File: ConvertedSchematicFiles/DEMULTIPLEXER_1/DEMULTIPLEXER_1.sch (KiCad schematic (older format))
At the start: 16 parts, among them U1 74393, U2 74151A

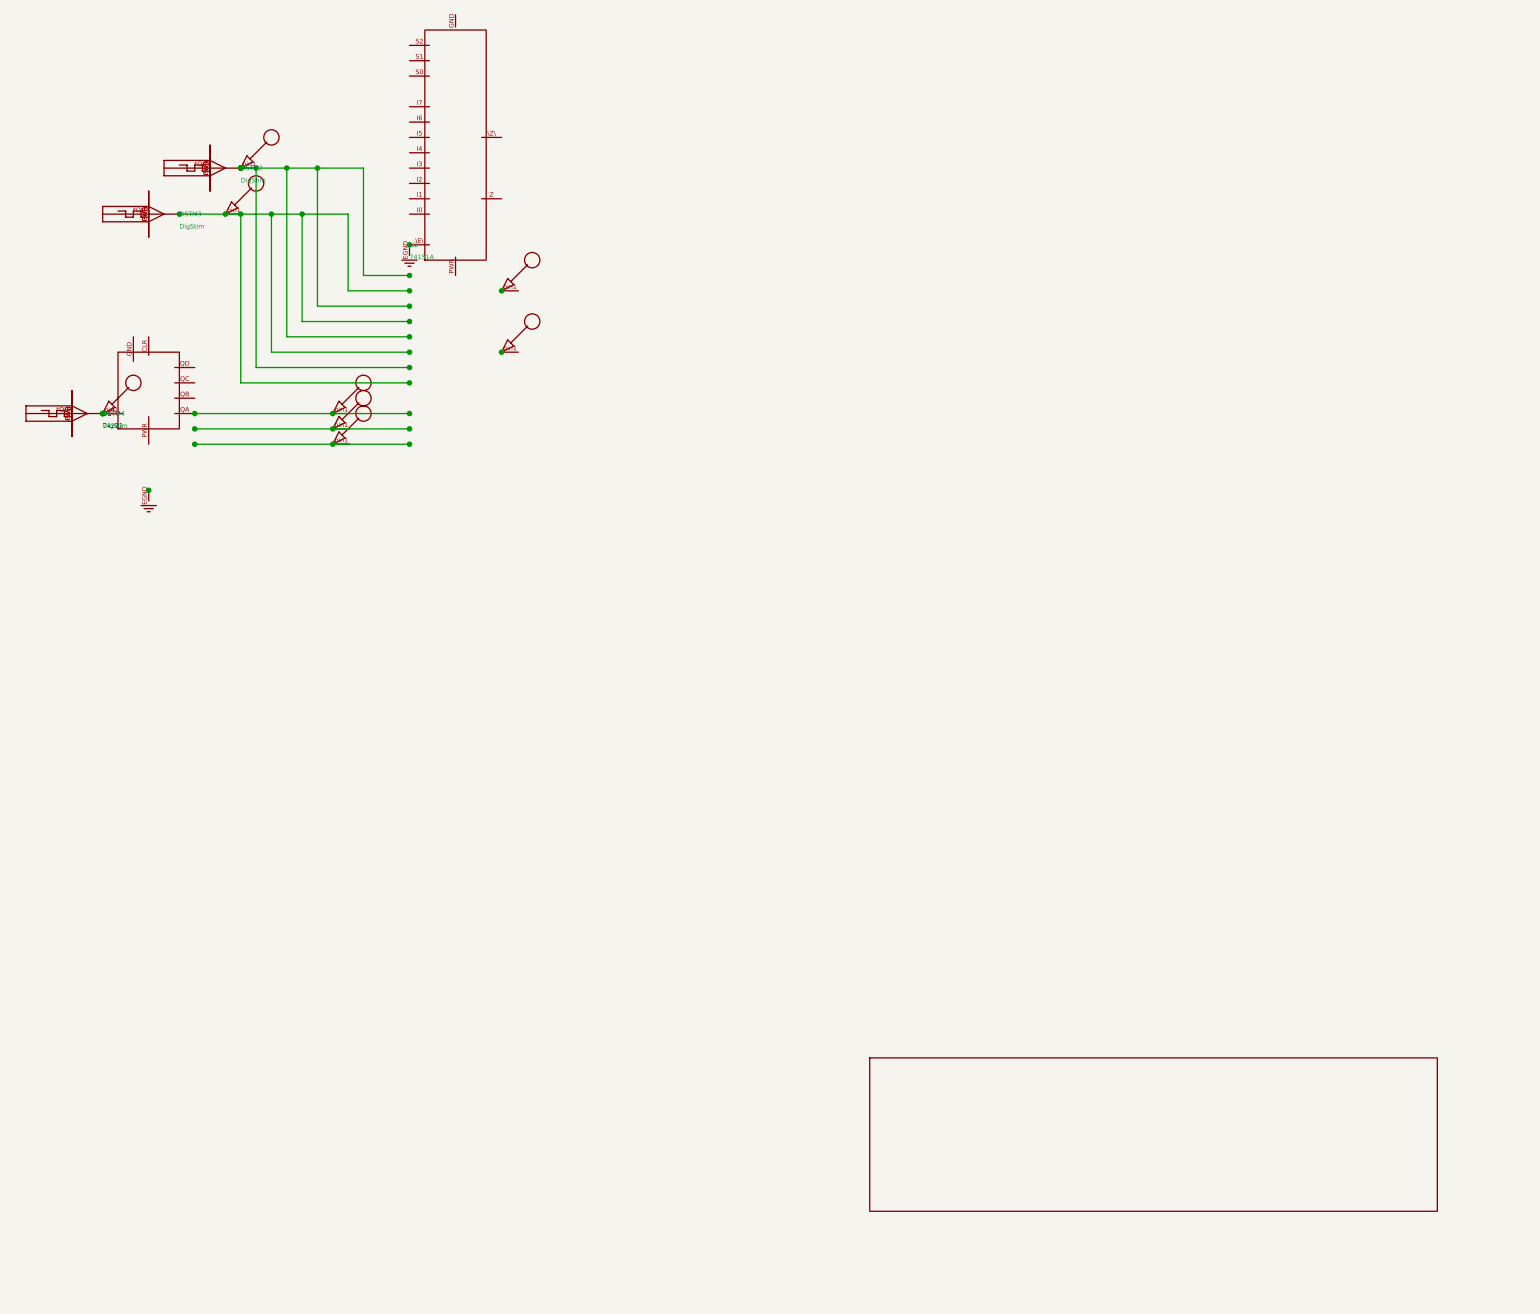
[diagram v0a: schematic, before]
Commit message: Excluded some components. These no longer appear after conversion. When calling shell commands, filenames are in "quotes"
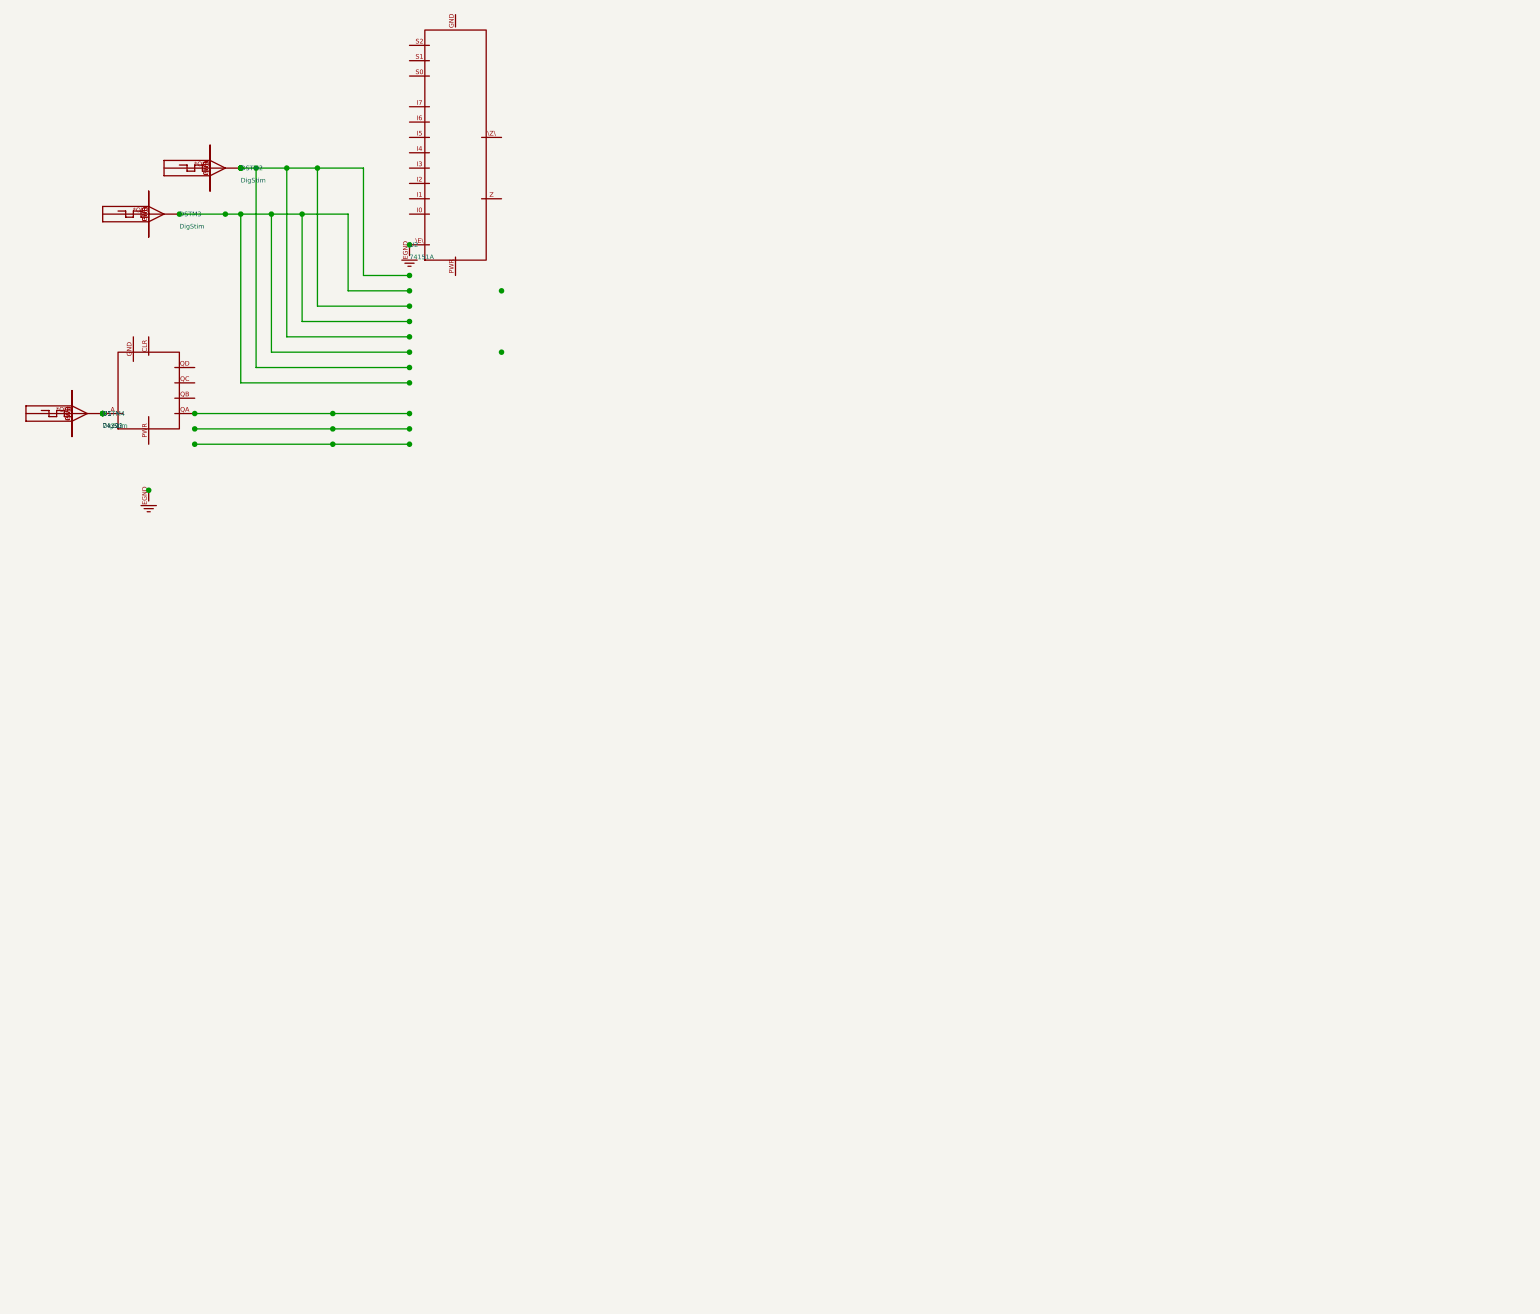
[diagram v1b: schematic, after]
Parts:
- removed nodeMarker (x8): nodeMarker, symbol NODEMARKER_PSPICE
- removed titleblk: titleblk, symbol TITLEBLK_PSPICE
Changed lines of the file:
@@
-	1    0    0    1
-$EndComp
-$Comp
-L TITLEBLK_PSPICE titleblk
-U 1 1 39760492
-P 9700 7200
-F 0 "titleblk" H 19400 14400 30  0001 L CNN
-F 1 "titleblk" H 19400 14480 30  0001 L CNN
-	1    9700 7200
-	1    0    0    1
-$EndComp
-$Comp
-L NODEMARKER_PSPICE nodeMarker
-U 1 1 66516649
-P 2500 2200
-F 0 "nodeMarker" H 5000 4400 30  0001 L CNN
-F 1 "nodeMarker" H 5000 4480 30  0001 L CNN
-	1    2500 2200
-	1    0    0    1
-$EndComp
-$Comp
-L NODEMARKER_PSPICE nodeMarker
-U 1 1 29641421
-P 2500 2100
-F 0 "nodeMarker" H 5000 4200 30  0001 L CNN
-F 1 "nodeMarker" H 5000 4280 30  0001 L CNN
-	1    2500 2100
-	1    0    0    1
-$EndComp
-$Comp
-L NODEMARKER_PSPICE nodeMarker
-U 1 1 45202362
-P 2500 2000
-F 0 "nodeMarker" H 5000 4000 30  0001 L CNN
-F 1 "nodeMarker" H 5000 4080 30  0001 L CNN
-	1    2500 2000
-	1    0    0    1
-$EndComp
-$Comp
-L NODEMARKER_PSPICE nodeMarker
-U 1 1 10490027
-P 1800 700
-F 0 "nodeMarker" H 3600 1400 30  0001 L CNN
-F 1 "nodeMarker" H 3600 1480 30  0001 L CNN
-	1    1800 700
-	1    0    0    1
-$EndComp
-$Comp
-L NODEMARKER_PSPICE nodeMarker
-U 1 1 73368690
-P 1900 400
-F 0 "nodeMarker" H 3800 800 30  0001 L CNN
-F 1 "nodeMarker" H 3800 880 30  0001 L CNN
-	1    1900 400
-	1    0    0    1
-$EndComp
-$Comp
-L NODEMARKER_PSPICE nodeMarker
-U 1 1 32520059
-P 3600 1600
-F 0 "nodeMarker" H 7200 3200 30  0001 L CNN
-F 1 "nodeMarker" H 7200 3280 30  0001 L CNN
-	1    3600 1600
-	1    0    0    1
-$EndComp
-$Comp
-L NODEMARKER_PSPICE nodeMarker
-U 1 1 74897763
-P 3600 1200
-F 0 "nodeMarker" H 7200 2400 30  0001 L CNN
-F 1 "nodeMarker" H 7200 2480 30  0001 L CNN
-	1    3600 1200
-	1    0    0    1
-$EndComp
-$Comp
-L NODEMARKER_PSPICE nodeMarker
-U 1 1 87513926
-P 1000 2000
-F 0 "nodeMarker" H 2000 4000 30  0001 L CNN
-F 1 "nodeMarker" H 2000 4080 30  0001 L CNN
-	1    1000 2000
 	1    0    0    1
 $EndComp

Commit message: Ports issue fixed. Now annotation for ports is #PWR? function added "itos"
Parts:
- removed EGND (x2): EGND, symbol EGND_PSPICE
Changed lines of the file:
@@
 $EndDescr
 $Comp
-L EGND_PSPICE EGND
+L EGND_PSPICE #PWR1
 U 1 1 14289383
 P 1300 2500
-F 0 "EGND" H 2600 5000 30  0001 L CNN
+F 0 "#PWR1" H 2600 5000 30  0001 L CNN
 F 1 "EGND" H 2600 5080 30  0001 L CNN
 	1    1300 2500
@@
 $EndComp
 $Comp
-L EGND_PSPICE EGND
+L EGND_PSPICE #PWR2
 U 1 1 46930886
 P 3000 900
-F 0 "EGND" H 6000 1800 30  0001 L CNN
+F 0 "#PWR2" H 6000 1800 30  0001 L CNN
 F 1 "EGND" H 6000 1880 30  0001 L CNN
 	1    3000 900

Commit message: Added LICENSE.txt
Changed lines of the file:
@@
 $EndDescr
 $Comp
-L EGND_PSPICE #PWR1
+L GND #PWR1
 U 1 1 14289383
 P 1300 2500
@@
 $EndComp
 $Comp
-L EGND_PSPICE #PWR2
+L GND #PWR2
 U 1 1 46930886
 P 3000 900

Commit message: Orientation fix. Library components are now inverted, with +ve y axis going up. In Schematic files, +ve y axis is downwards. This is how the KiCad libraries are. As a result of the above fixed, the converted GND is now oriented correctly.
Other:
- moved on the sheet: U1, U2
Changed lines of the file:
@@
 F 1 "EGND" H 2600 5080 30  0001 L CNN
 	1    1300 2500
-	1    0    0    1
+	1    0    0    -1
 $EndComp
 $Comp
@@
 F 1 "EGND" H 6000 1880 30  0001 L CNN
 	1    3000 900
-	1    0    0    1
+	1    0    0    -1
 $EndComp
 $Comp
@@
 F 1 "DigStim" H 1500 780 30  0000 L CNN
 	1    1500 700
-	1    0    0    1
+	1    0    0    -1
 $EndComp
 $Comp
@@
 F 1 "DigStim" H 1900 480 30  0000 L CNN
 	1    1900 400
-	1    0    0    1
+	1    0    0    -1
 $EndComp
 $Comp
@@
 F 1 "74151A" H 3000 980 30  0000 L CNN
 	1    3000 900
-	1    0    0    1
+	1    0    0    -1
 $EndComp
 $Comp
@@
 F 1 "74393" H 1000 2080 30  0000 L CNN
 	1    1000 2000
-	1    0    0    1
+	1    0    0    -1
 $EndComp
 $Comp
@@
 F 1 "DigStim" H 1000 2080 30  0000 L CNN
 	1    1000 2000
-	1    0    0    1
+	1    0    0    -1
 $EndComp
 Wire Wire Line

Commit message: Removed the use of exec, wrote basename function, made integration with eSim easier.
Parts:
- added nodeMarker (x8): nodeMarker, symbol nodeMarker_PSPICE
- added titleblk: titleblk, symbol titleblk_PSPICE
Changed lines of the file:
@@
-EESchema Schematic File Version 2  date Sunday 27 June 1999 01:55:42 AM IST
+EESchema Schematic File Version 2  date
 LIBS:power
 LIBS:device
@@
 LIBS:contrib
 LIBS:valves
-LIBS:ConvertedSchematicFiles/DEMULTIPLEXER_1-cache
 EELAYER 25  0
 EELAYER END
@@
 Sheet 1 1
 Title ""
-Date "27 Jun 1999"
+Date ""
 Rev ""
 Comp ""
@@
 	1    1000 2000
 	1    0    0    -1
+$EndComp
+$Comp
+L titleblk_PSPICE titleblk
+U 1 1 39760492
+P 9700 7200
+F 0 "titleblk" H 19400 14400 30  0001 L CNN
+F 1 "titleblk" H 19400 14480 30  0001 L CNN
+	1    9700 7200
+	1    0    0    -1
+$EndComp
+$Comp
+L nodeMarker_PSPICE nodeMarker
+U 1 1 66516649
+P 2500 2200
+F 0 "nodeMarker" H 5000 4400 30  0001 L CNN
+F 1 "nodeMarker" H 5000 4480 30  0001 L CNN
+	1    2500 2200
+	1    0    0    -1
+$EndComp
+$Comp
+L nodeMarker_PSPICE nodeMarker
+U 1 1 29641421
+P 2500 2100
+F 0 "nodeMarker" H 5000 4200 30  0001 L CNN
+F 1 "nodeMarker" H 5000 4280 30  0001 L CNN
+	1    2500 2100
+	1    0    0    -1
+$EndComp
+$Comp
+L nodeMarker_PSPICE nodeMarker
+U 1 1 45202362
+P 2500 2000
+F 0 "nodeMarker" H 5000 4000 30  0001 L CNN
+F 1 "nodeMarker" H 5000 4080 30  0001 L CNN
+	1    2500 2000
+	1    0    0    -1
+$EndComp
+$Comp
+L nodeMarker_PSPICE nodeMarker
+U 1 1 10490027
+P 1800 700
+F 0 "nodeMarker" H 3600 1400 30  0001 L CNN
+F 1 "nodeMarker" H 3600 1480 30  0001 L CNN
+	1    1800 700
+	1    0    0    -1
+$EndComp
+$Comp
+L nodeMarker_PSPICE nodeMarker
+U 1 1 73368690
+P 1900 400
+F 0 "nodeMarker" H 3800 800 30  0001 L CNN
+F 1 "nodeMarker" H 3800 880 30  0001 L CNN
+	1    1900 400
+	1    0    0    -1
+$EndComp
+$Comp
+L nodeMarker_PSPICE nodeMarker
+U 1 1 32520059
+P 3600 1600
+F 0 "nodeMarker" H 7200 3200 30  0001 L CNN
+F 1 "nodeMarker" H 7200 3280 30  0001 L CNN
+	1    3600 1600
+	1    0    0    -1
+$EndComp
+$Comp
+L nodeMarker_PSPICE nodeMarker
+U 1 1 74897763
+P 3600 1200
+F 0 "nodeMarker" H 7200 2400 30  0001 L CNN
+F 1 "nodeMarker" H 7200 2480 30  0001 L CNN
+	1    3600 1200
+	1    0    0    -1
+$EndComp
+$Comp
+L nodeMarker_PSPICE nodeMarker
+U 1 1 87513926
+P 1000 2000
+F 0 "nodeMarker" H 2000 4000 30  0001 L CNN
+F 1 "nodeMarker" H 2000 4080 30  0001 L CNN
+	1    1000 2000
+	1    0    0    -1
